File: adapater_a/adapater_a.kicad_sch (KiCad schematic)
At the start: 30 parts, among them J101 Conn_01x03, J102 CN8, J103 CN9, J104 CN7, J105 CN10, U101 TPS5430DDA, U102 TLV2372

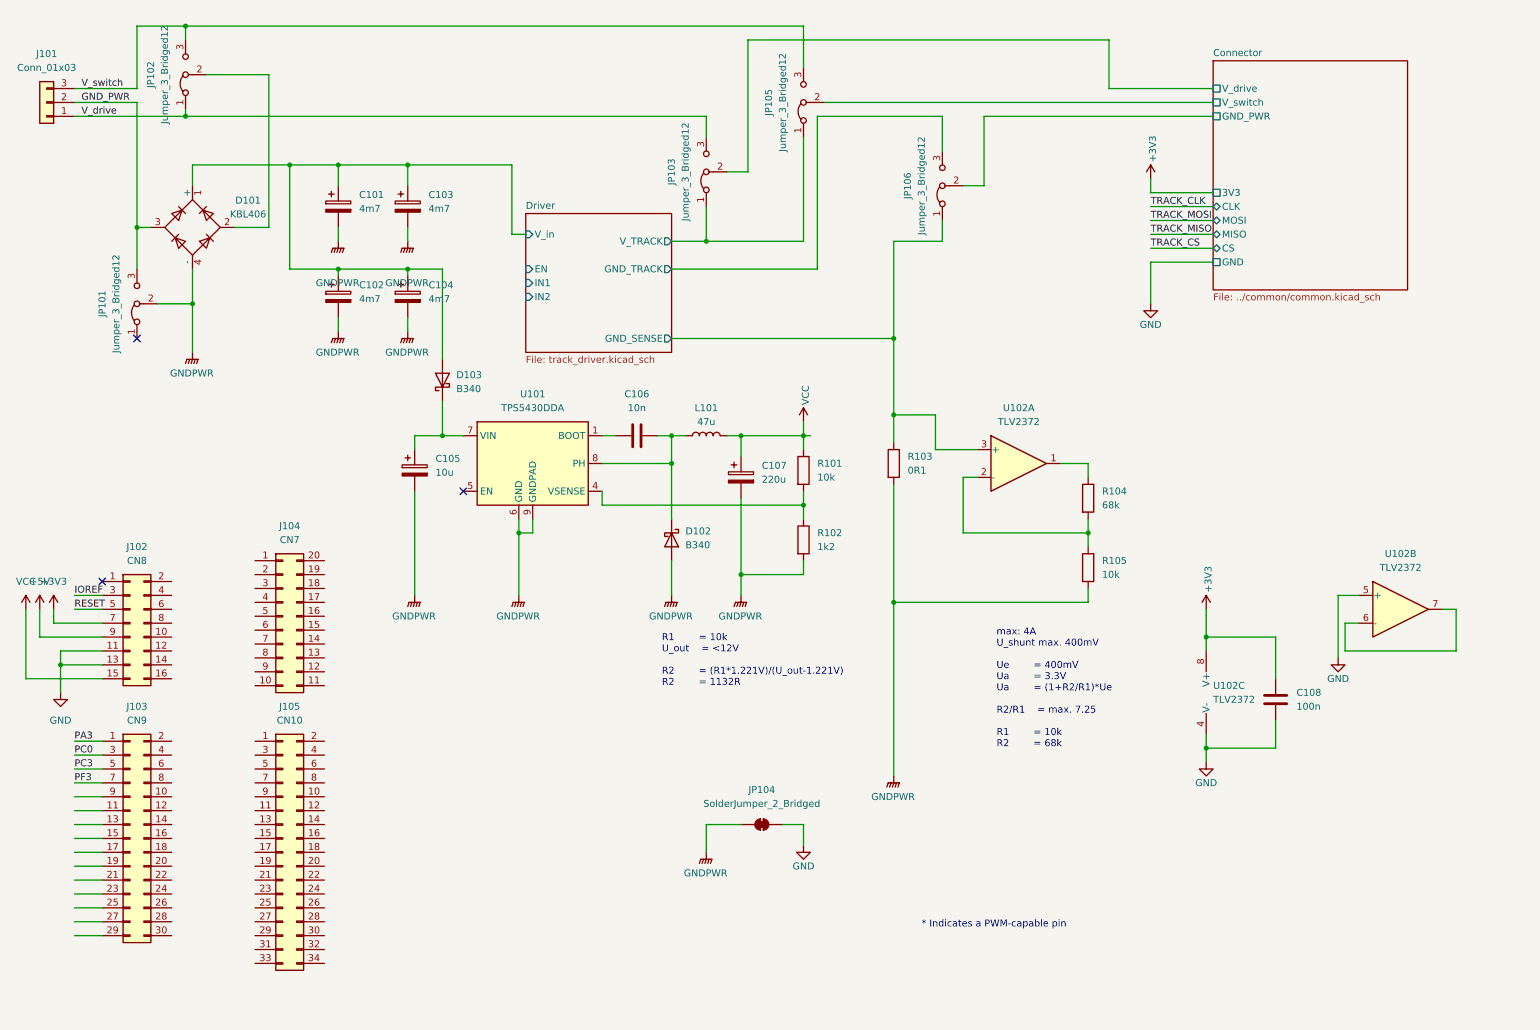
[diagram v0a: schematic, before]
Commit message: Add voltage messurement
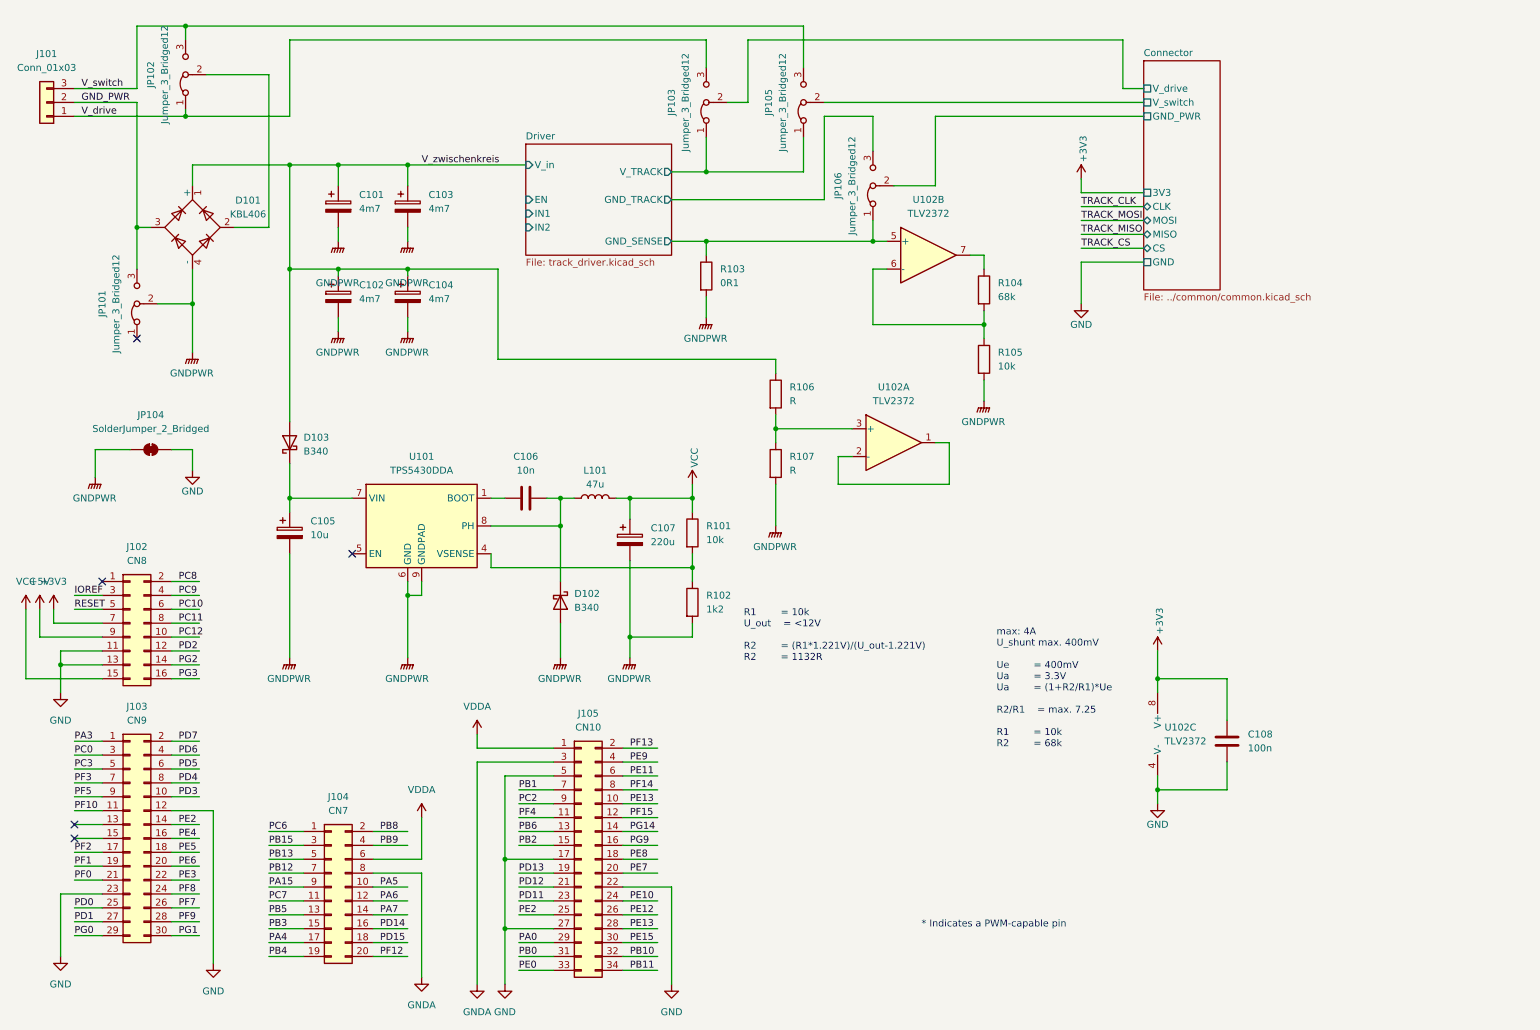
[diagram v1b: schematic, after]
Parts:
- removed J104: CN7, Connector_PinHeader_2.54mm:PinHeader_2x10_P2.54mm_Vertical, symbol Connector_Generic:Conn_02x10_Counter_Clockwise
- added J104: CN7, Connector_PinHeader_2.54mm:PinHeader_2x10_P2.54mm_Vertical, symbol Connector_Generic:Conn_02x10_Odd_Even
- added R106, R107: R, Resistor_SMD:R_0805_2012Metric, symbol Device:R
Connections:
- net Driver/GND_SENSE: now also U102.5 (+); no longer U102.3 (+)
- net GND: now also J103.12 (Pin_12), J103.23 (Pin_23), J105.17 (Pin_17), J105.22 (Pin_22), J105.27 (Pin_27), J105.5 (Pin_5); no longer U102.5 (+)
- net GNDPWR: now also R107.2
- net at U102.1: now also U102.2 (-); no longer R104.1
- net at R104.2, R105.1: now also U102.6 (-); no longer U102.2 (-)
- net at U102.7: now also R104.1; no longer U102.6 (-)
- net PC12: now reaches J102.10 (Pin_10)
- net PD2: now reaches J102.12 (Pin_12)
- net PG2: now reaches J102.14 (Pin_14)
- net PG3: now reaches J102.16 (Pin_16)
- net PC8: now reaches J102.2 (Pin_2)
- net PC9: now reaches J102.4 (Pin_4)
- net PC10: now reaches J102.6 (Pin_6)
- net PC11: now reaches J102.8 (Pin_8)
- net VDDA: now reaches J105.1 (Pin_1)
- net VDDA: now also J104.6 (Pin_6)
- net PE13: now reaches J105.10 (Pin_10)
- net PE13: now also J105.28 (Pin_28)
- net PF4: now reaches J105.11 (Pin_11)
- net PF15: now reaches J105.12 (Pin_12)
- net PB6: now reaches J105.13 (Pin_13)
- net PG14: now reaches J105.14 (Pin_14)
- net PB2: now reaches J105.15 (Pin_15)
- net PG9: now reaches J105.16 (Pin_16)
- net PE8: now reaches J105.18 (Pin_18)
- net PD13: now reaches J105.19 (Pin_19)
- net PF13: now reaches J105.2 (Pin_2)
- net PE7: now reaches J105.20 (Pin_20)
- net PD12: now reaches J105.21 (Pin_21)
- net PD11: now reaches J105.23 (Pin_23)
- net PE10: now reaches J105.24 (Pin_24)
- net PE2: now reaches J105.25 (Pin_25)
- net PE2: now also J103.14 (Pin_14)
- net PE12: now reaches J105.26 (Pin_26)
- net PA0: now reaches J105.29 (Pin_29)
- net GNDA: now reaches J105.3 (Pin_3)
- net GNDA: now also J104.8 (Pin_8)
- net PE15: now reaches J105.30 (Pin_30)
- net PB0: now reaches J105.31 (Pin_31)
- net PB10: now reaches J105.32 (Pin_32)
- net PE0: now reaches J105.33 (Pin_33)
- net PB11: now reaches J105.34 (Pin_34)
- net PE9: now reaches J105.4 (Pin_4)
- net PE11: now reaches J105.6 (Pin_6)
- net PB1: now reaches J105.7 (Pin_7)
- net PF14: now reaches J105.8 (Pin_8)
- net PC2: now reaches J105.9 (Pin_9)
- net PD3: now reaches J103.10 (Pin_10)
- net PF10: now reaches J103.11 (Pin_11)
- net PE4: now reaches J103.16 (Pin_16)
- net PF2: now reaches J103.17 (Pin_17)
- net PE5: now reaches J103.18 (Pin_18)
- net PF1: now reaches J103.19 (Pin_19)
- net PD7: now reaches J103.2 (Pin_2)
- net PE6: now reaches J103.20 (Pin_20)
- net PF0: now reaches J103.21 (Pin_21)
- net PE3: now reaches J103.22 (Pin_22)
- net PF8: now reaches J103.24 (Pin_24)
- net PD0: now reaches J103.25 (Pin_25)
- net PF7: now reaches J103.26 (Pin_26)
- net PD1: now reaches J103.27 (Pin_27)
- net PF9: now reaches J103.28 (Pin_28)
- net PG0: now reaches J103.29 (Pin_29)
- net PG1: now reaches J103.30 (Pin_30)
- net PD6: now reaches J103.4 (Pin_4)
- net PD5: now reaches J103.6 (Pin_6)
- net PD4: now reaches J103.8 (Pin_8)
- net PF5: now reaches J103.9 (Pin_9)
- net Driver/V_in renamed V_zwischenkreis
- net V_zwischenkreis: now also R106.1
- new net: R106.2, R107.1, U102.3 (+)
- new net PA15: J104.9 (Pin_9)
- new net PA4: J104.17 (Pin_17)
- new net PA5: J104.10 (Pin_10)
- new net PA6: J104.12 (Pin_12)
- new net PA7: J104.14 (Pin_14)
- new net PB12: J104.7 (Pin_7)
- new net PB13: J104.5 (Pin_5)
- new net PB15: J104.3 (Pin_3)
- new net PB3: J104.15 (Pin_15)
- new net PB4: J104.19 (Pin_19)
- new net PB5: J104.13 (Pin_13)
- new net PB8: J104.2 (Pin_2)
- new net PB9: J104.4 (Pin_4)
- new net PC6: J104.1 (Pin_1)
- new net PC7: J104.11 (Pin_11)
- new net PD14: J104.16 (Pin_16)
- new net PD15: J104.18 (Pin_18)
- new net PF12: J104.20 (Pin_20)
- no-connect marks 3 -> 5
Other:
- moved on the sheet: C105, C106, C107, C108, D102, D103, J105, JP103, JP104, JP106, L101, R101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

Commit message: Update adapter A
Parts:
- added C109, C110: 10n, Capacitor_SMD:C_0805_2012Metric, symbol Device:C
- added D104, D107: gr, LED_SMD:LED_0805_2012Metric, symbol Device:LED
- added D105: red, LED_SMD:LED_0805_2012Metric, symbol Device:LED
- added D106: yl, LED_SMD:LED_0805_2012Metric, symbol Device:LED
- added R108, R109, R110, R111: R, Resistor_SMD:R_0805_2012Metric, symbol Device:R
- added R112, R113: 68k, Resistor_SMD:R_0805_2012Metric, symbol Device:R
- added SW101: SW_DIP_x10, Button_Switch_SMD:SW_DIP_SPSTx10_Slide_KingTek_DSHP10TS_W7.62mm_P1.27mm, symbol Switch:SW_DIP_x10
- J104: LCSC (none) -> C5116480
- R106: value R -> 10k; LCSC (none) -> C17414
- R107: value R -> 820; LCSC (none) -> C23253
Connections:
- net PC10 is gone; now on net TRACK_CLK: J102.6 (Pin_6)
- net PC11 is gone; now on net TRACK_MISO: J102.8 (Pin_8)
- net PC12 is gone; now on net TRACK_MOSI: J102.10 (Pin_10)
- net PD2 is gone; now on net TRACK_CS: J102.12 (Pin_12)
- net GND: now also C109.1, C110.1, D104.1 (K), D105.1 (K), D106.1 (K), D107.1 (K), SW101.1, SW101.10, SW101.2, SW101.3, SW101.4, SW101.5, SW101.6, SW101.7, SW101.8, SW101.9
- net PA15: now also SW101.16
- net PA4: now also SW101.12
- net PB12: now also SW101.17
- net PB13: now also SW101.18
- net PB15: now also SW101.19
- net PB3: now also SW101.13
- net PB4: now also SW101.11
- net PB5: now also SW101.14
- net PC6: now also SW101.20
- net PC7: now also SW101.15
- net PC9: now also R109.1
- net PE0: now also R108.1
- net PE13: no longer J105.28 (Pin_28)
- net PE2: no longer J105.25 (Pin_25)
- net PG2: now also R110.1
- net PG3: now also R111.1
- net at U102.1, U102.2 (-): now also R112.1
- net at R104.1, U102.7: now also R113.1
- net PA3 renamed ADC_current
- net ADC_current: now also C110.2, R113.2
- net PC0 renamed ADC_voltage
- net ADC_voltage: now also C109.2, R112.2
- new net: D106.2 (A), R110.2
- new net: D107.2 (A), R111.2
- new net: D104.2 (A), R108.2
- new net: D105.2 (A), R109.2
- new net PE14: J105.28 (Pin_28)
- new net PE2a: J105.25 (Pin_25)
- no-connect marks 5 -> 70
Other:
- moved on the sheet: J104, J105, JP103, JP105, JP106, R104, R105, U102B

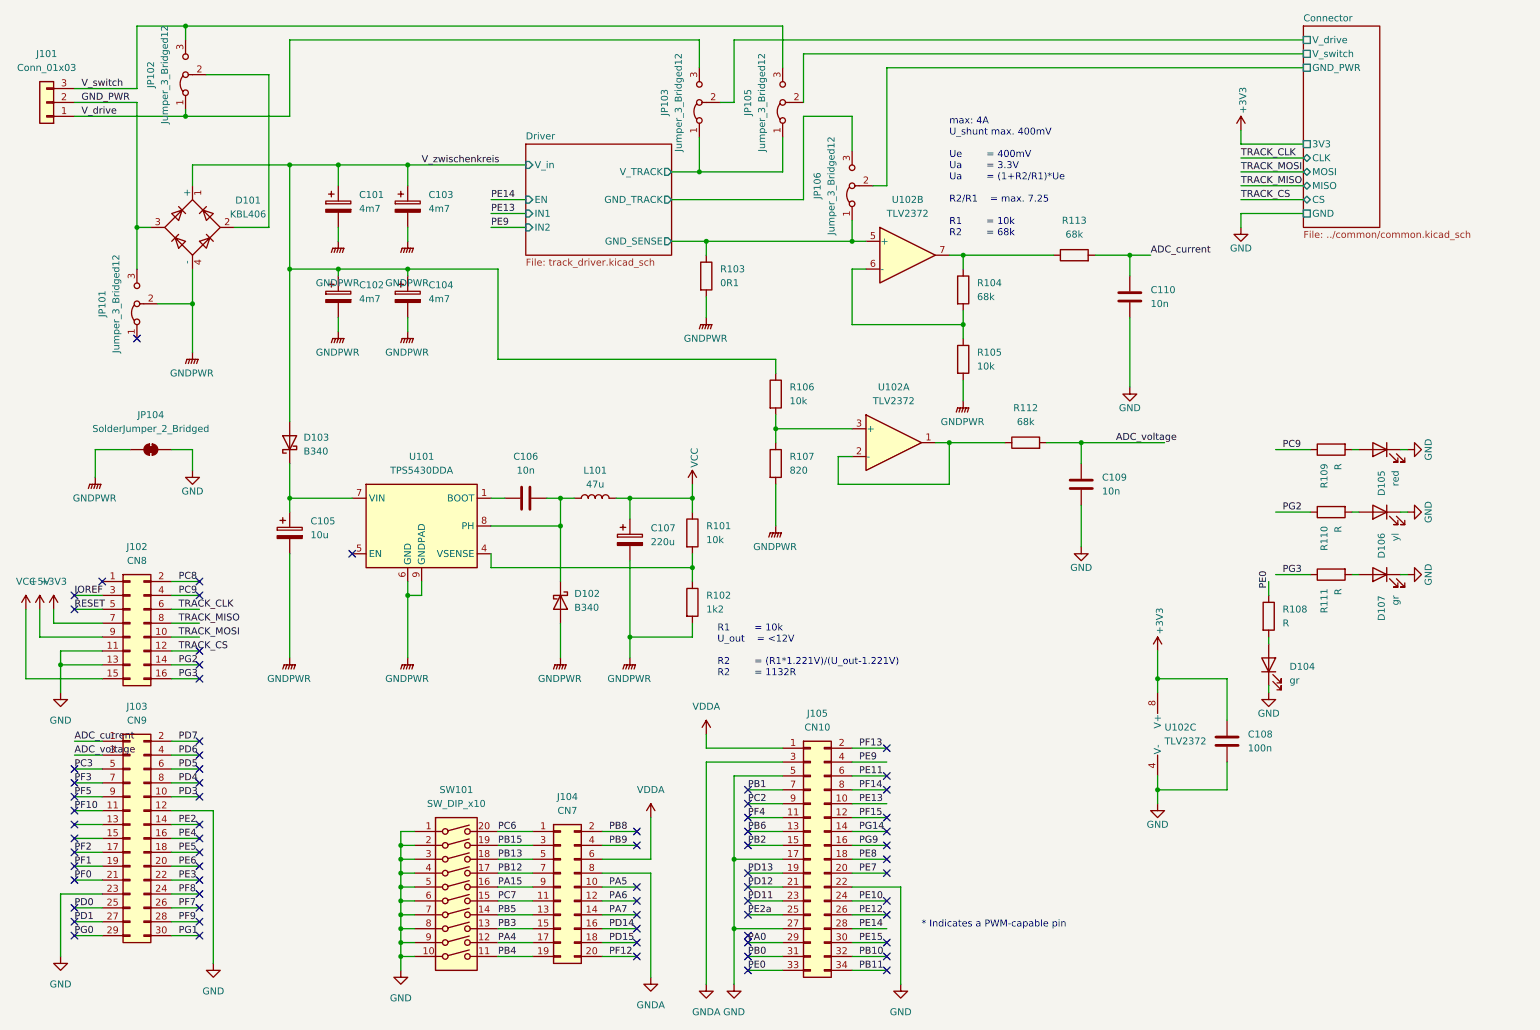
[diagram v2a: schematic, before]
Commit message: Nicer signal names
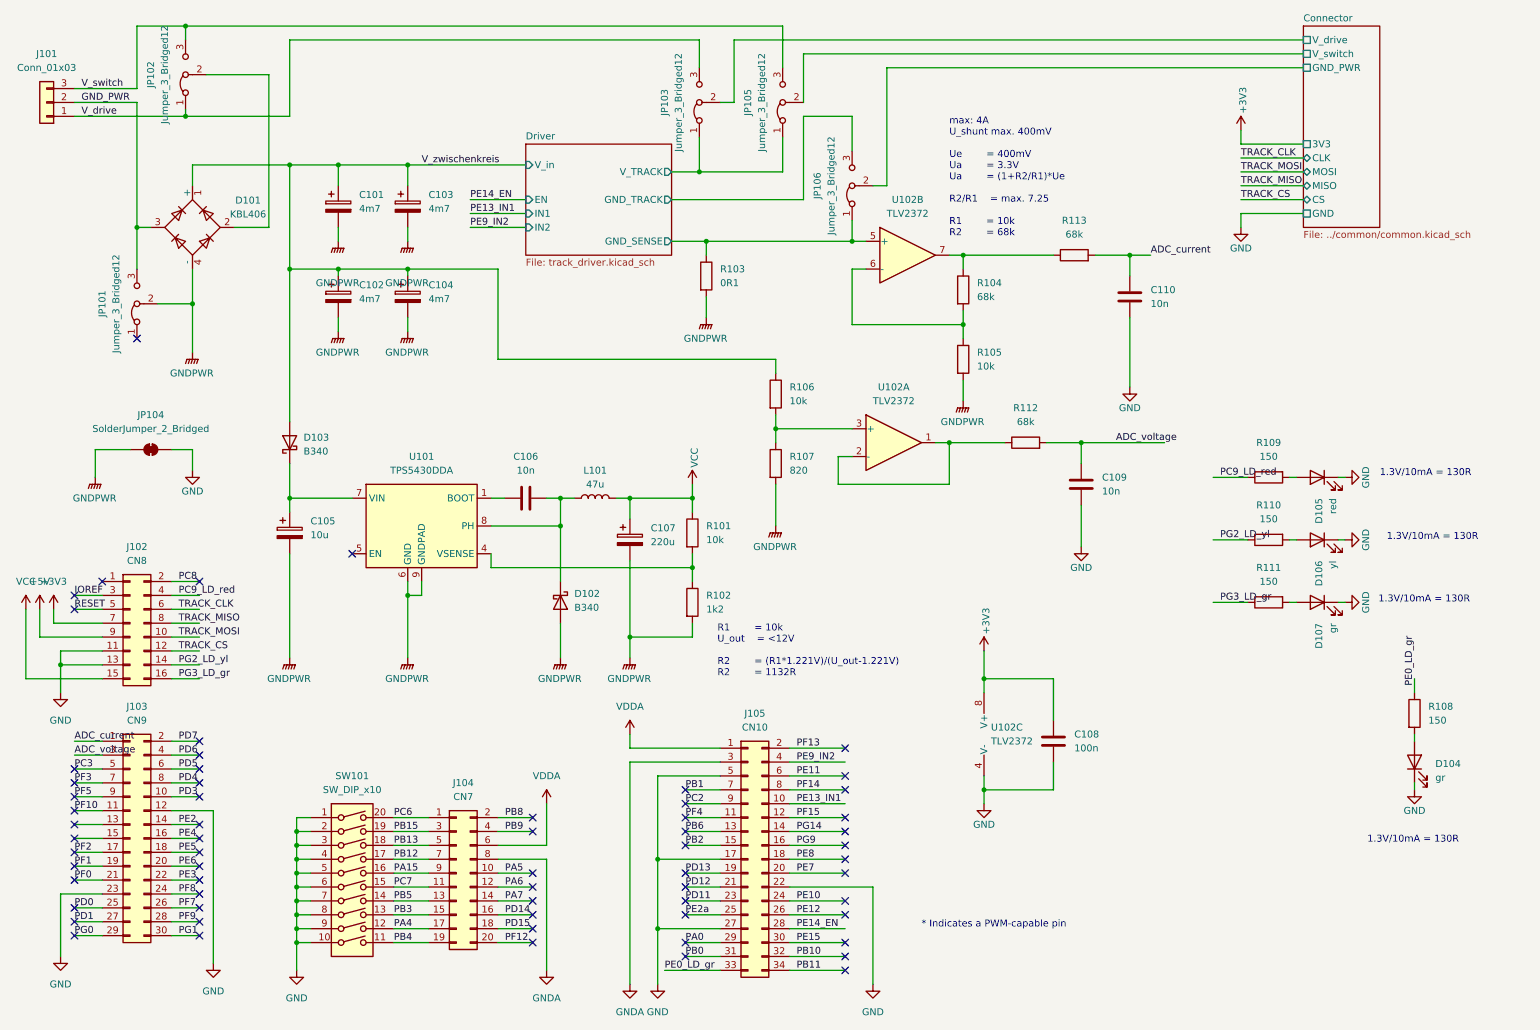
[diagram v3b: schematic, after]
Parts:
- R108, R109, R110, R111: value R -> 150; LCSC (none) -> C17471
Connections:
- net PC9 renamed PC9_LD_red
- net PE0 renamed PE0_LD_gr
- net PE13 renamed PE13_IN1
- net PE14 renamed PE14_EN
- net PE9 renamed PE9_IN2
- net PG2 renamed PG2_LD_yl
- net PG3 renamed PG3_LD_gr
- no-connect marks 70 -> 64
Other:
- note added: "1.3V/10mA = 130R"
- moved on the sheet: C108, D104, D105, D106, D107, J104, J105, R108, R109, R110, R111, SW101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
